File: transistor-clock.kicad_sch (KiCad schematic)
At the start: 49 parts, among them J1 Screw_Terminal_01x02, J2 Conn_01x01_Socket, J3 Conn_01x01_Socket, J4 Conn_01x01_Socket, J5 Conn_01x01_Socket, J6 Conn_01x01_Socket, J7 Conn_01x01_Socket, Q1 MMBT3904, Q2 MMBT3904, Q3 DMP3099L, Q4 2N7002, Q5 MMBT3904, Q6 MMBT3904, Q7 MMBT3904, Q8 MMBT3904, T1 Transformer_1P_SS, T2 CL2-20-12

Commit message: dunno
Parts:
- removed Q3: DMP3099L, Package_TO_SOT_SMD:SOT-23, symbol Transistor_FET:DMP3099L
- added Q87: AO3401A, Package_TO_SOT_SMD:SOT-23, symbol Transistor_FET:AO3401A
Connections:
- net VDD: now also Q87.2 (S)
- net at C3.2, Q2.3 (C), Q4.1 (G)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: now also Q87.1 (G)
- net at Q4.3 (D), Q5.1 (B): now also Q87.3 (D)
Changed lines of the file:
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@@
 	)
 	(junction
+		(at 88.9 120.65)
+		(diameter 0)
+		(color 0 0 0 0)
+	)
+	(junction
 		(at 223.52 29.21)
 		(diameter 0)
@@
 	)
 	(junction
-		(at 88.9 130.81)
-		(diameter 0)
-		(color 0 0 0 0)
-	)
-	(junction
 		(at 100.33 44.45)
 		(diameter 0)
@@
 	)
 	(junction
+		(at 88.9 130.81)
+		(diameter 0)
+		(color 0 0 0 0)
+	)
+	(junction
 		(at 53.34 120.65)
 		(diameter 0)
@@
 	)
 	(junction
-		(at 88.9 120.65)
-		(diameter 0)
-		(color 0 0 0 0)
-	)
-	(junction
 		(at 100.33 29.21)
 		(diameter 0)
@@
 	(wire
 		(pts
+			(xy 88.9 120.65) (xy 118.11 120.65)
+		)
+		(stroke
+			(width 0)
+			(type default)
+		)
+	)
+	(wire
+		(pts
 			(xy 33.02 128.27) (xy 33.02 134.62)
 		)
@@
 	(wire
 		(pts
-			(xy 88.9 120.65) (xy 118.11 120.65)
-		)
-		(stroke
-			(width 0)
-			(type default)
-		)
-	)
-	(wire
-		(pts
 			(xy 68.58 55.88) (xy 68.58 62.23)
 		)
@@
 	)
 	(symbol
-		(lib_id "Transistor_FET:DMP3099L")
-		(at 86.36 125.73 0)
-		(mirror x)
-		(unit 1)
-		(exclude_from_sim no)
-		(in_bom yes)
-		(on_board yes)
-		(dnp no)
-		(fields_autoplaced yes)
-		(property "Reference" "Q3"
-			(at 91.567 124.5178 0)
-			(effects
-				(font
-					(size 1.27 1.27)
-				)
-				(justify left)
-			)
-		)
-		(property "Value" "DMP3099L"
-			(at 91.567 126.9421 0)
-			(effects
-				(font
-					(size 1.27 1.27)
-				)
-				(justify left)
-			)
-		)
-		(property "Footprint" "Package_TO_SOT_SMD:SOT-23"
-			(at 91.44 123.825 0)
-			(effects
-				(font
-					(size 1.27 1.27)
-					(italic yes)
-				)
-				(justify left)
-				(hide yes)
-			)
-		)
-		(property "Datasheet" "https://www.diodes.com/assets/Datasheets/DMP3099L.pdf"
-			(at 91.44 121.92 0)
-			(effects
-				(font
-					(size 1.27 1.27)
-				)
-				(justify left)
-				(hide yes)
-			)
-		)
-		(property "Description" "-3.8A Id, -30V Vds, P-Channel MOSFET, SOT-23"
-			(at 86.36 125.73 0)
-			(effects
-				(font
-					(size 1.27 1.27)
-				)
-				(hide yes)
-			)
-		)
-		(pin "2"
-		)
-		(pin "3"
-		)
-		(pin "1"
-		)
-		(instances
-			(project "transistor-clock"
-				(path "/ce10d5bc-995e-4952-aa76-0a08f713a0f2"
-					(reference "Q3")
-					(unit 1)
-				)
-			)
-		)
-	)
-	(symbol
 		(lib_id "power:VDD")
 		(at 148.59 55.88 0)
@@
 					(unit 1)
 				)
+			)
+		)
+	)
+	(symbol
+		(lib_id "Transistor_FET:AO3401A")
+		(at 86.36 125.73 0)
+		(mirror x)
+		(unit 1)
+		(exclude_from_sim no)
+		(in_bom yes)
+		(on_board yes)
+		(dnp no)
+		(fields_autoplaced yes)
+		(property "Reference" "Q87"
+			(at 91.567 124.5178 0)
+			(effects
+				(font
+					(size 1.27 1.27)
+				)
+				(justify left)
+			)
+		)
+		(property "Value" "AO3401A"
+			(at 91.567 126.9421 0)
+			(effects
+				(font
+					(size 1.27 1.27)
+				)
+				(justify left)
+			)
+		)
+		(property "Footprint" "Package_TO_SOT_SMD:SOT-23"
+			(at 91.44 123.825 0)
+			(effects
+				(font
+					(size 1.27 1.27)
+					(italic yes)
+				)
+				(justify left)
+				(hide yes)
+			)
+		)
+		(property "Datasheet" "http://www.aosmd.com/pdfs/datasheet/AO3401A.pdf"
+			(at 91.44 121.92 0)
+			(effects
+				(font
+					(size 1.27 1.27)
+				)
+				(justify left)
+				(hide yes)
+			)
+		)
+		(property "Description" "-4.0A Id, -30V Vds, P-Channel MOSFET, SOT-23"
+			(at 86.36 125.73 0)
+			(effects
+				(font
+					(size 1.27 1.27)
+				)
+				(hide yes)
+			)
+		)
+		(pin "2"
+		)
+		(pin "1"
+		)
+		(pin "3"
+		)
+		(instances
+			(project ""
+				(path "/ce10d5bc-995e-4952-aa76-0a08f713a0f2"
+					(reference "Q87")
+					(unit 1)
+				)

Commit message: added LCSC part numbers
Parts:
- C1, C3: LCSC Part # (none) -> C57112
- C2, C4, C5, C6, C7, C8, C9: footprint Capacitor_SMD:C_0603_1608Metric -> Capacitor_Tantalum_SMD:CP_EIA-3528-12_Kemet-T; LCSC Part # (none) -> C16133
- D1, D2, D3, D4: LCSC Part # (none) -> C47921
- Q1, Q2, Q5, Q6, Q7, Q8: LCSC Part # (none) -> C20526v
- Q4: LCSC Part # (none) -> C8545
- Q87: LCSC Part # (none) -> C15127
- R1: LCSC Part # (none) -> C177577
- R10, R8, R9: LCSC Part # (none) -> C23204
- R11: LCSC Part # (none) -> C25971
- R12: LCSC Part # (none) -> C158942
- R2: LCSC Part # (none) -> C23058
- R3, R6: LCSC Part # (none) -> C22809
- R4, R5: LCSC Part # (none) -> C73805
- R7: LCSC Part # (none) -> C21190

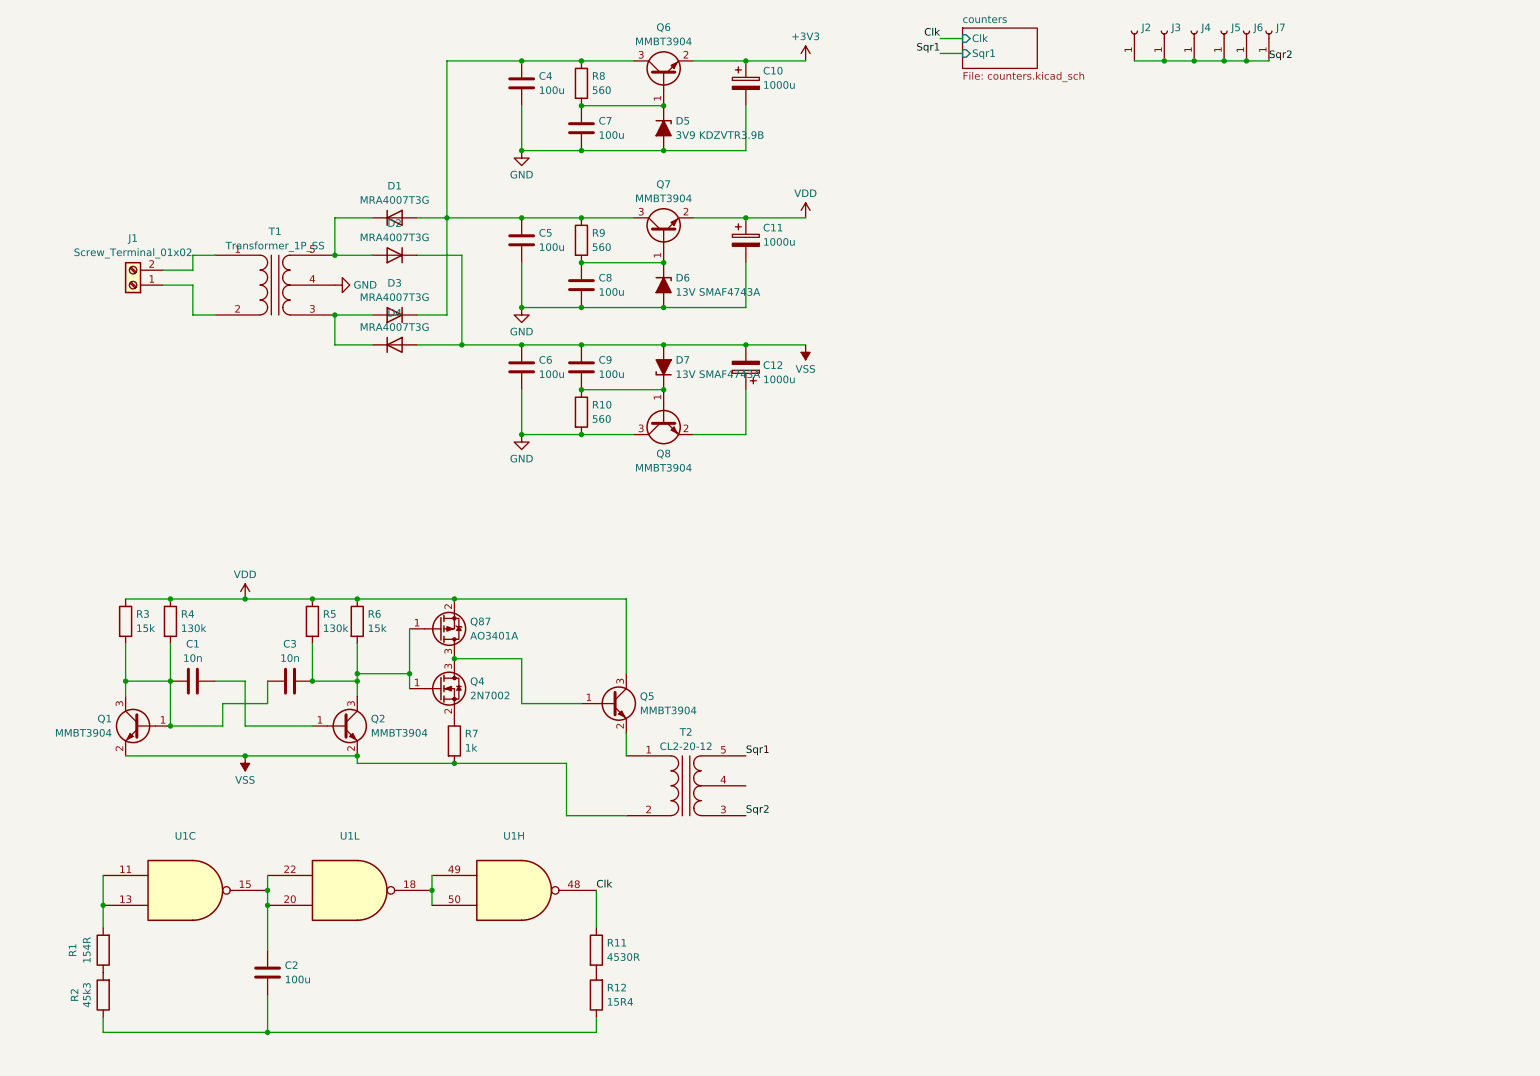
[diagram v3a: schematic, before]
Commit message: switched clock to bjt astable multivibrator
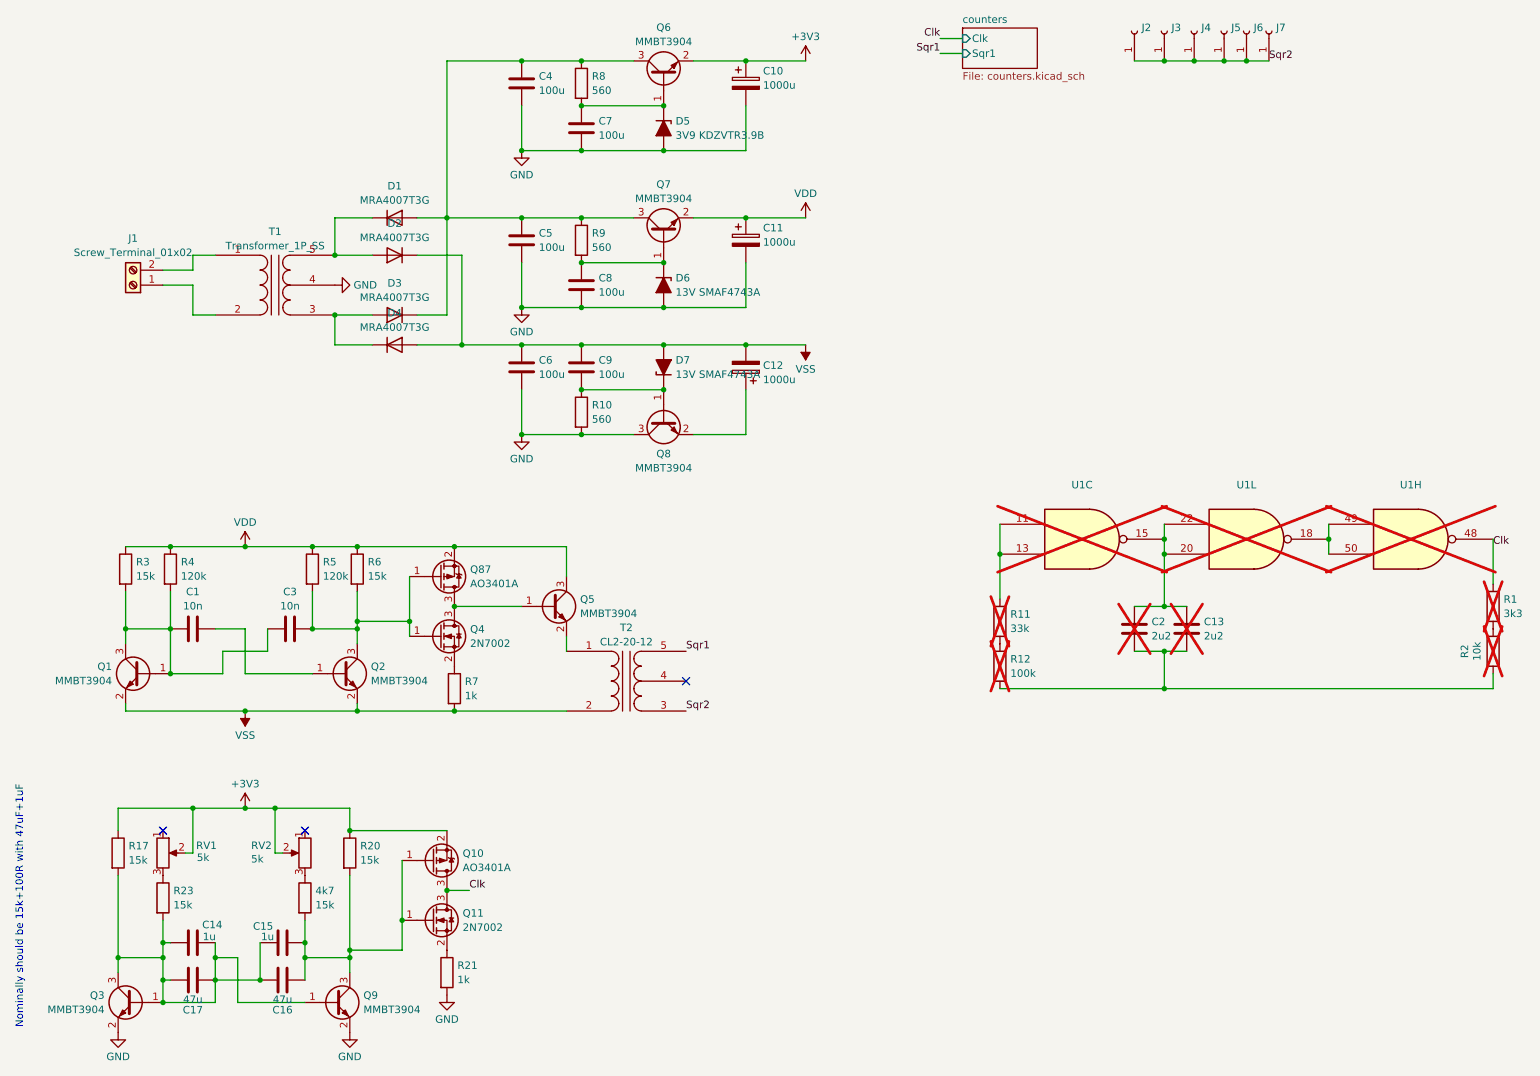
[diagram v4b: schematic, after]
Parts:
- added 4k7, R17, R20, R23: 15k, Resistor_SMD:R_0402_1005Metric, symbol Device:R
- added C13: 2u2, Capacitor_Tantalum_SMD:CP_EIA-3528-12_Kemet-T, symbol Device:C
- added C14, C15: 1u, Capacitor_SMD:C_0603_1608Metric, symbol Device:C
- added C16, C17: 47u, Capacitor_SMD:C_0805_2012Metric, symbol Device:C
- added Q10: AO3401A, Package_TO_SOT_SMD:SOT-23, symbol Transistor_FET:AO3401A
- added Q11: 2N7002, Package_TO_SOT_SMD:SOT-23, symbol Transistor_FET:2N7002
- added Q3, Q9: MMBT3904, Package_TO_SOT_SMD:SOT-23, symbol Transistor_BJT:MMBT3904
- added R21: 1k, Resistor_SMD:R_0402_1005Metric, symbol Device:R
- added RV1, RV2: 5k, Potentiometer_SMD:Potentiometer_Bourns_3214J_Horizontal, symbol Device:R_Potentiometer
- C10, C11, C12: footprint Capacitor_SMD:CP_Elec_5x3 -> Capacitor_SMD:CP_Elec_10x10.5; LCSC Part # (none) -> C3359
- C2: value 100u -> 2u2; LCSC Part # C16133 -> C23630; now not fitted
- R1: value 154R -> 3k3; LCSC Part # C177577 -> C22978; now not fitted
- R11: value 4530R -> 33k; LCSC Part # C25971 -> C4216; now not fitted
- R12: value 15R4 -> 100k; LCSC Part # C158942 -> C25803; now not fitted
- R2: value 45k3 -> 10k; LCSC Part # C23058 -> C25804; now not fitted
- R4, R5: value 130k -> 120k; LCSC Part # C73805 -> C25808
- U1: now not fitted
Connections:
- net +3V3: now also Q10.2 (S), R17.1, R20.1, RV1.2, RV2.2
- net Clk: now also R1.2, Q10.3 (D), Q11.3 (D); no longer R11.1
- net GND: now also Q3.2 (E), Q9.2 (E), R21.2
- net at C2.1, R12.1, R2.1: now also C13.1
- net at C2.2, U1.15, U1.20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: now also C13.2
- net at U1.11, U1.13: now also R11.1; no longer R1.2
- new net: C14.1, C14.2, C15.1, C16.1, C17.1, C17.2, Q3.1 (B), Q3.3 (C), Q9.1 (B), R17.2, R23.2
- new net: 4k7.2, C15.2, C16.2, Q10.1 (G), Q11.1 (G), Q9.3 (C), R20.2
- new net: 4k7.1, RV2.3
- new net: R23.1, RV1.3
- new net: Q11.2 (S), R21.1
- no-connect marks 0 -> 3
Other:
- note added: "Nominally should be 15k+100R with 47uF+1uF"
- moved on the sheet: C1, C3, Q1, Q2, Q4, Q5, Q87, R3, R4, R5, R6, R7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

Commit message: changed some components to lcsc parts
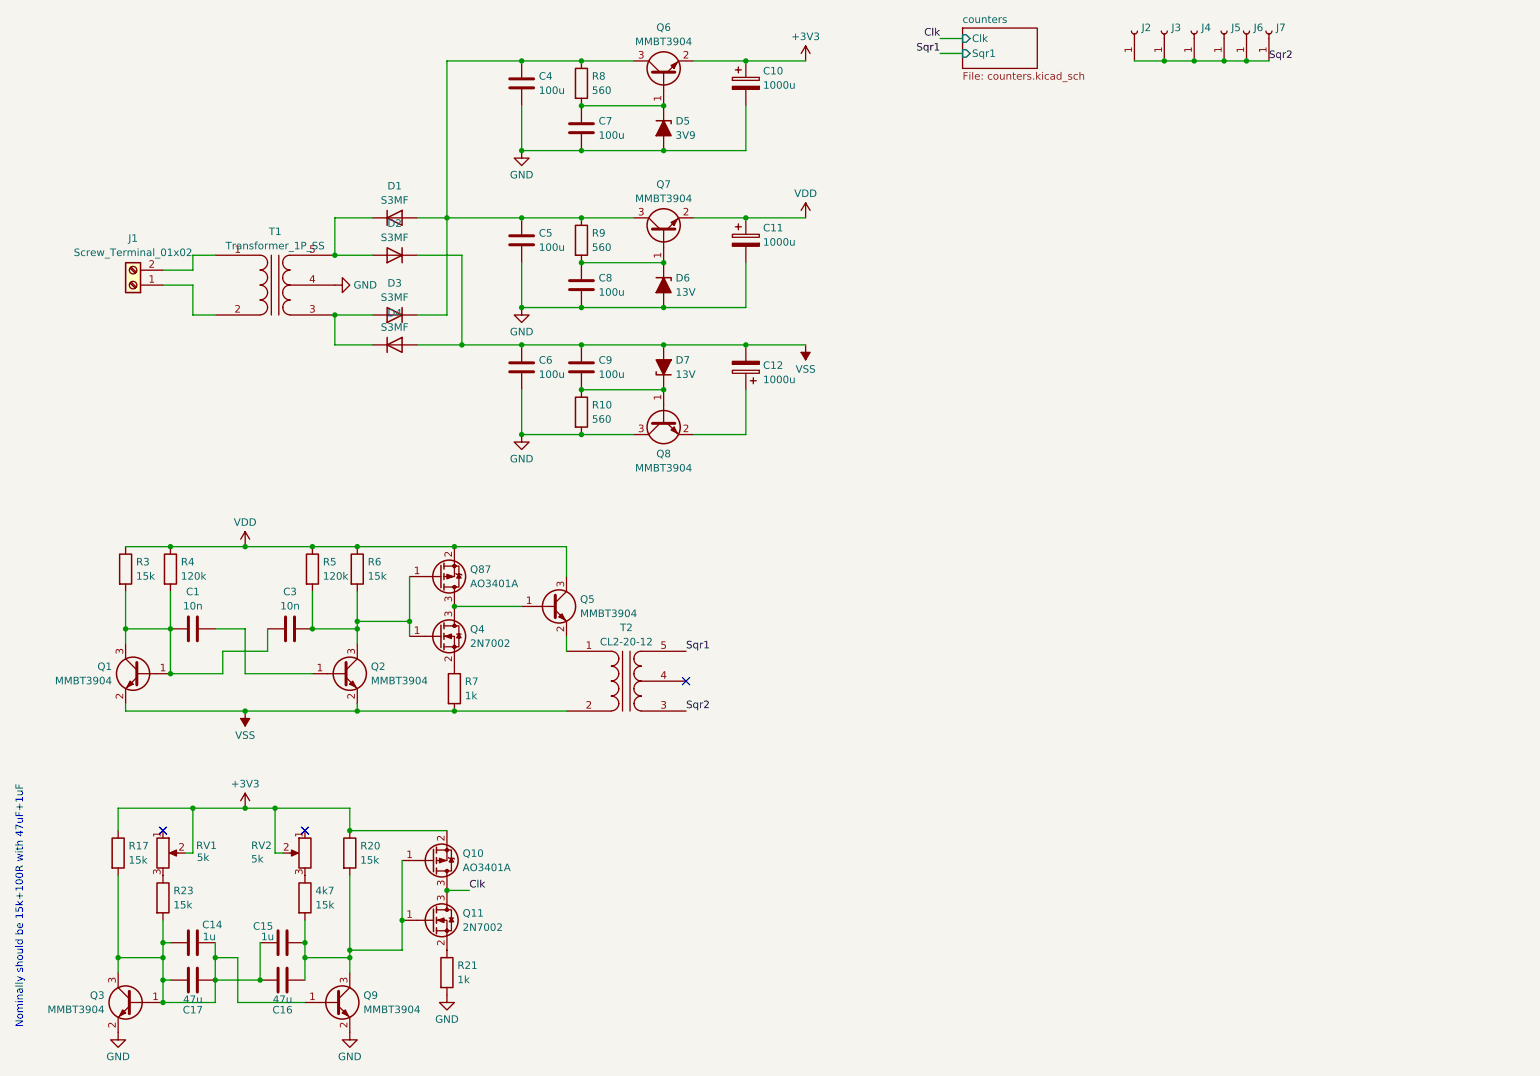
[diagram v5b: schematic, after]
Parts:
- removed C13, C2: 2u2, Capacitor_Tantalum_SMD:CP_EIA-3528-12_Kemet-T, symbol Device:C
- removed R1: 3k3, Resistor_SMD:R_0402_1005Metric, symbol Device:R
- removed R11: 33k, Resistor_SMD:R_0402_1005Metric, symbol Device:R
- removed R12: 100k, Resistor_SMD:R_0402_1005Metric, symbol Device:R
- removed R2: 10k, Resistor_SMD:R_0402_1005Metric, symbol Device:R
- removed U1: ~, symbol custom:BDC_nands
- D1, D2, D3, D4: value MRA4007T3G -> S3MF; footprint Diode_SMD:D_SMA -> Diode_SMD:D_SMA-SMB_Universal_Handsoldering; LCSC Part # C47921 -> C64874
- D5: value 3V9 KDZVTR3.9B -> 3V9; LCSC Part # (none) -> C2114
- D6, D7: value 13V SMAF4743A -> 13V; footprint Diode_SMD:Vishay_SMPA -> Diode_SMD:D_SOD-123; LCSC Part # (none) -> C21547

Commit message: added footprints for modules
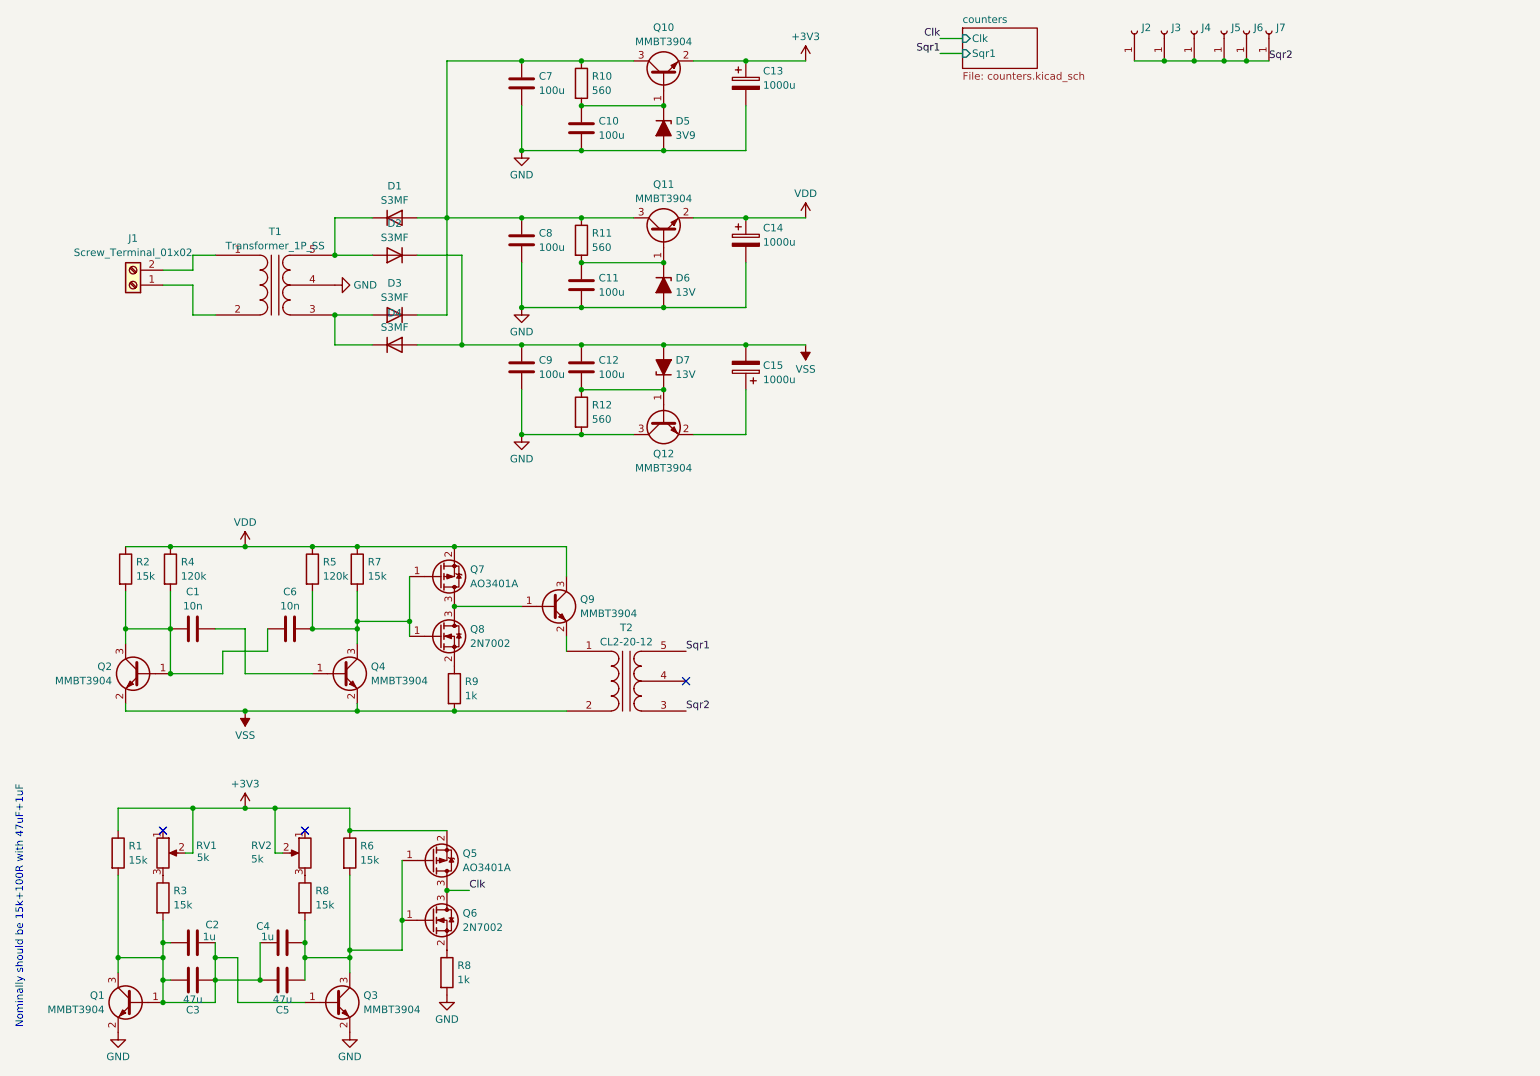
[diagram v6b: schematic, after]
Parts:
- D1, D2, D3, D4: footprint Diode_SMD:D_SMA-SMB_Universal_Handsoldering -> Diode_SMD:D_SMA
- renumbered C7 to C10, C8 to C11, C9 to C12, C10 to C13, C11 to C14, C12 to C15, C14 to C2, C17 to C3, C15 to C4, C16 to C5, C3 to C6, C4 to C7, C5 to C8, C6 to C9, Q3 to Q1, Q6 to Q10, Q7 to Q11, Q8 to Q12, Q1 to Q2, Q9 to Q3, Q2 to Q4, Q10 to Q5, Q11 to Q6, Q87 to Q7, Q4 to Q8, Q5 to Q9, R17 to R1, R8 to R10, R9 to R11, R10 to R12, R3 to R2, R23 to R3, R20 to R6, R6 to R7, R21 to R8, 4k7 to R8, R7 to R9
